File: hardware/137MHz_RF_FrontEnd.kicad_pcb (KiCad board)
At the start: 2 copper layers, 85.3 x 40.2 mm, 39 parts, among them J1 Conn_Coaxial, J2 Conn_Coaxial, J3 Conn_01x02_Pin, Q1 AO3401A, U1 PGA-103

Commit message: Update & applied changes
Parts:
- removed R4, R5: 300, Resistor_SMD:R_0603_1608Metric_Pad0.98x0.95mm_HandSolder
- removed R6: 18, Resistor_SMD:R_0603_1608Metric_Pad0.98x0.95mm_HandSolder
- moved J2 8.11 mm to (145.5, 101.5)
- moved C9 7.96 mm to (129.4, 102.4)
- moved L13 7.91 mm to (136.1, 101.6)
- moved L14 7.91 mm to (140.8, 102.4)
- moved C10 7.90 mm to (132.4, 101.6)
- moved C14 7.90 mm to (138.9, 102.4)
- moved L11 7.90 mm to (127.4, 102.4)
- moved J3 1.02 mm to (136.5, 87.5)
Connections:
- C15 pad 1: Net-(C15-Pad1) -> Net-(C10-Pad2)
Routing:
- net GND: track 5.09 -> 0.00 mm, vias 125 -> 183
- net Net-(C15-Pad1): track 3.77 -> 0.00 mm
- net Net-(C10-Pad2): track 8.22 -> 5.93 mm
- net Net-(J3-Pin_1): track 9.31 -> 8.34 mm
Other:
- board size 85.3 x 40.2 mm -> 75.8 x 40.2 mm
- board text added: "3rd Order Butterworth band-pass 120Mhz-175MHz"
- board text added: "5th Order Cauer Notch 88MHz-108MHz"
- board text added: "FM-Notch + LNA + BPF"
- board text added: "PGA-103+ 22db Gain"
- board text added: "RF IN"
- board text added: "RF OUT"

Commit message: ad
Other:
- board text added: "3rd Order Butterworth band-pass 125Mhz-170MHz"
- board text removed: "3rd Order Butterworth band-pass 120Mhz-175MHz"
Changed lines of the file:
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@@
 		)
 	)
-	(gr_text "3rd Order Butterworth band-pass\n120Mhz-175MHz"
+	(gr_text "3rd Order Butterworth band-pass\n125Mhz-170MHz"
 		(at 126.83 111.25 0)
 		(layer "F.SilkS")

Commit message: update
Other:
- board text removed: "3rd Order Butterworth band-pass 125Mhz-170MHz"
- board text removed: "5th Order Cauer Notch 88MHz-108MHz"
- board text removed: "FM-Notch + LNA + BPF"
- board text removed: "PGA-103+ 22db Gain"
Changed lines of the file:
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@@
 		(layer "Edge.Cuts")
-	)
-	(gr_text "5th Order Cauer Notch\n88MHz-108MHz"
-		(at 86.14 110.89 0)
-		(layer "F.SilkS")
-		(effects
-			(font
-				(size 0.8 0.8)
-				(thickness 0.15)
-				(bold yes)
-			)
-			(justify left bottom)
-		)
-	)
-	(gr_text "PGA-103+\n22db Gain"
-		(at 116.13 107.46 0)
-		(layer "F.SilkS")
-		(effects
-			(font
-				(size 0.8 0.8)
-				(thickness 0.15)
-				(bold yes)
-			)
-			(justify left bottom)
-		)
-	)
-	(gr_text "3rd Order Butterworth band-pass\n125Mhz-170MHz"
-		(at 126.83 111.25 0)
-		(layer "F.SilkS")
-		(effects
-			(font
-				(size 0.8 0.8)
-				(thickness 0.15)
-				(bold yes)
-			)
-			(justify left bottom)
-		)
-	)
-	(gr_text "FM-Notch + LNA + BPF"
-		(at 81.26 91.43 0)
-		(layer "F.SilkS")
-		(effects
-			(font
-				(size 0.9 0.9)
-				(thickness 0.225)
-				(bold yes)
-			)
-			(justify left bottom)
-		)
 	)
 	(gr_text "RF OUT"

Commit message: updated values of L
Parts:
- L4: value 150nH -> 120nH
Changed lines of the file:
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@@
 			)
 		)
-		(property "Value" "150nH"
+		(property "Value" "120nH"
 			(at 0 1.43 90)
 			(layer "F.Fab")

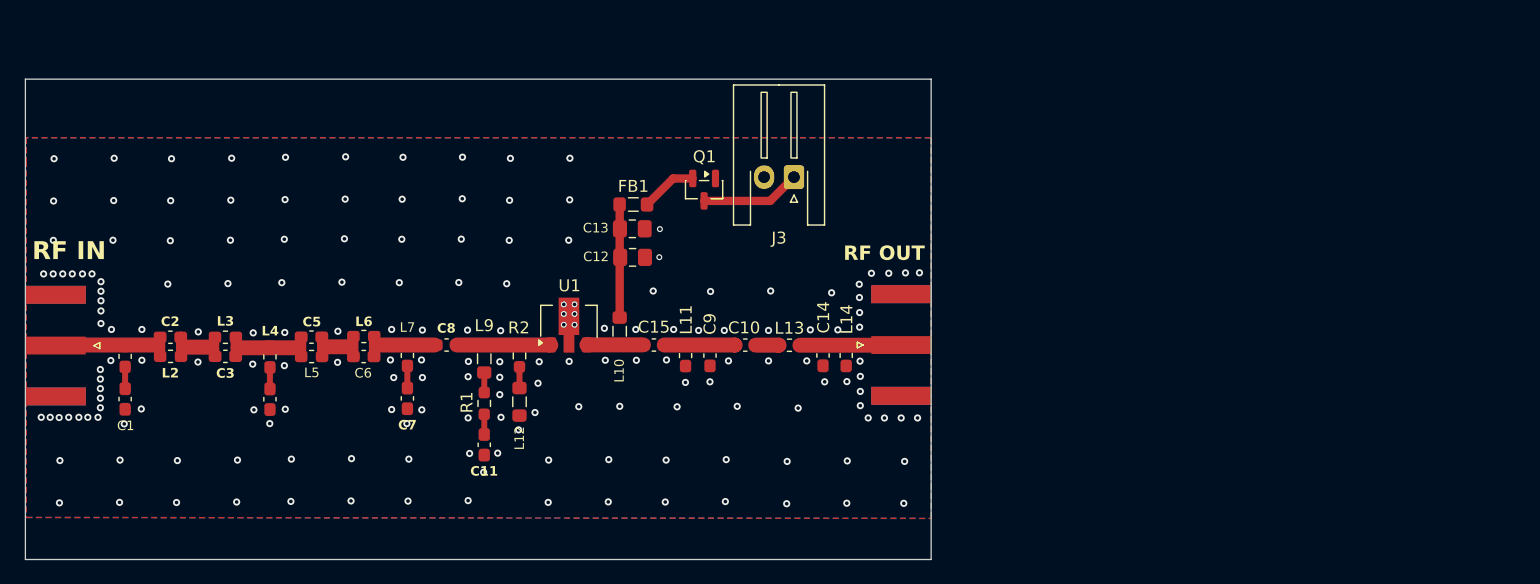
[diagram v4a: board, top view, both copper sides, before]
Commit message: update/addedLDO
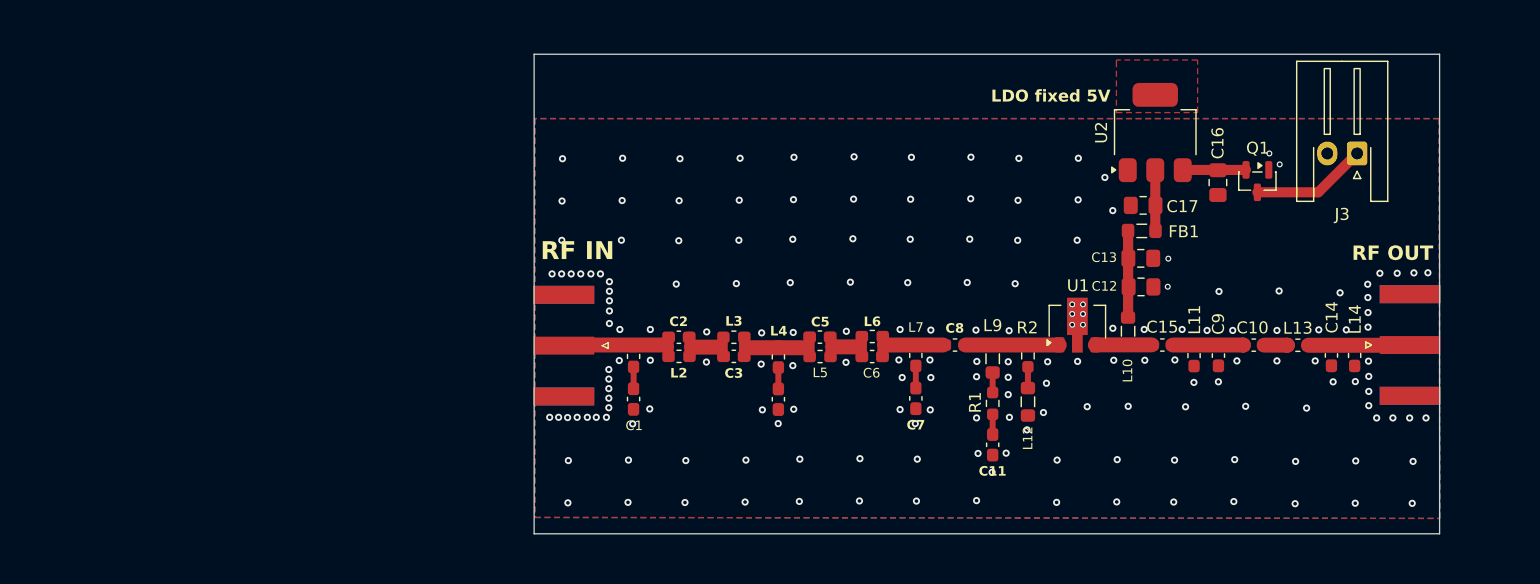
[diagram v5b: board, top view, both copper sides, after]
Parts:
- added C16: 10uF, Capacitor_SMD:C_0805_2012Metric_Pad1.18x1.45mm_HandSolder, F.Cu at (171.9, 88.0)
- added C17: 10uF, Capacitor_SMD:C_0805_2012Metric_Pad1.18x1.45mm_HandSolder, F.Cu at (165.7, 89.9)
- added U2: TLV1117-50, Package_TO_SOT_SMD:SOT-223, F.Cu at (166.7, 83.8)
- moved J3 47.2 mm to (183.6, 85.5)
- moved Q1 46.3 mm to (175.2, 87.8)
- moved C13 42.6 mm to (165.5, 94.3)
- moved C12 42.6 mm to (165.5, 96.7)
- moved FB1 42.6 mm to (165.6, 92.0)
- moved C15 42.6 mm to (167.3, 101.5)
- moved C2 42.6 mm to (126.8, 100.9)
- moved C5 42.6 mm to (138.6, 100.9)
- moved C7 42.6 mm to (146.7, 106.0)
- moved C9 42.6 mm to (172.0, 102.4)
- moved J1 42.6 mm to (117.2, 101.6)
- moved J2 42.6 mm to (188.0, 101.5)
- moved L10 42.6 mm to (164.4, 100.4)
- moved L12 42.6 mm to (156.1, 106.3)
- moved L3 42.6 mm to (131.4, 100.9)
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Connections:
- FB1 pad 1: Net-(Q1-S) -> Net-(U2-VO)
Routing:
- net Net-(U2-VO): track 0.00 -> 5.09 mm
- net Net-(C12-Pad1): track 9.46 -> 7.25 mm
- net Net-(J3-Pin_1): track 8.34 -> 9.70 mm
- net Net-(Q1-S): track 4.73 -> 5.27 mm
- net GND: vias 183 -> 186
- added copper zone on F.Cu, net Net-(U2-VO)
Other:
- board size 75.8 x 40.2 mm -> 75.8 x 40.1 mm
- board text added: "LDO fixed 5V"

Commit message: update PCB
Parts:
- added -: -, LOGO, F.Cu at (127.6, 81.8)
- moved L12 6.92 mm to (162.9, 105.3), turned to 180 degrees
- moved J2 6.34 mm to (194.4, 101.5)
- moved C10 5.99 mm to (180.9, 101.6)
- moved C14 5.99 mm to (187.4, 102.4)
- moved L11 5.99 mm to (175.9, 102.4)
- moved L13 5.99 mm to (184.6, 101.6)
- moved L14 5.99 mm to (189.4, 102.4)
- moved C9 5.98 mm to (178.0, 102.4)
- moved L 5.87 mm to (170.3, 100.4)
- moved C 5.82 mm to (173.1, 101.5)
- moved C11 5.69 mm to (158.8, 109.9)
- moved C2 5.69 mm to (132.5, 100.9)
- moved C3 5.69 mm to (137.1, 102.5)
- moved C4 5.69 mm to (140.8, 106.1)
- moved C5 5.69 mm to (144.3, 100.9)
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- renumbered C15 to C, L10 to L
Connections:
- U2 pad 4: (no net) -> Net-(U2-VO)
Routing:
- net Net-(U2-VO): track 5.09 -> 11.0 mm
- net Net-(C12-Pad1): track 7.25 -> 10.7 mm
- net Net-(J3-Pin_1): track 9.70 -> 10.6 mm
- net GND: vias 186 -> 334
- removed copper zone on F.Cu, net Net-(U2-VO)
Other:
- board size 75.8 x 40.1 mm -> 76.4 x 41.3 mm
- board text added: "+"
- board text added: "-"
- board text added: "50Ω"
- board text added: "C"
- board text added: "CH"
- board text added: "DC"
